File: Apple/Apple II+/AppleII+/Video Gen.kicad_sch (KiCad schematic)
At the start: 51 parts, among them J18 Aux Video, K14 VIDEO OUT, Q3 2N3904, Q6 2N3904

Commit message: less than 1000 errors to go
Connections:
- net GND: now also A9.8 (GND)
- net SOFT5: no longer A11.10 (~{S}), A11.13 (~{R}), A11.2 (D), A11.3 (C)
- net ~{RAS}: now also B5.1 (~{CLR}), B8.1 (~{CLR}), B8.1 (~{CLR})
- new net Soft5: A11.10 (~{S}), A11.13 (~{R}), A11.2 (D), A11.3 (C)
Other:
- note added: "James TODO: Verify these are wired correctly"
- note added: "James Todo: Is this 555 wired correclty"
- moved on the sheet: B3, B5A, B8A, B8F, C15, R13

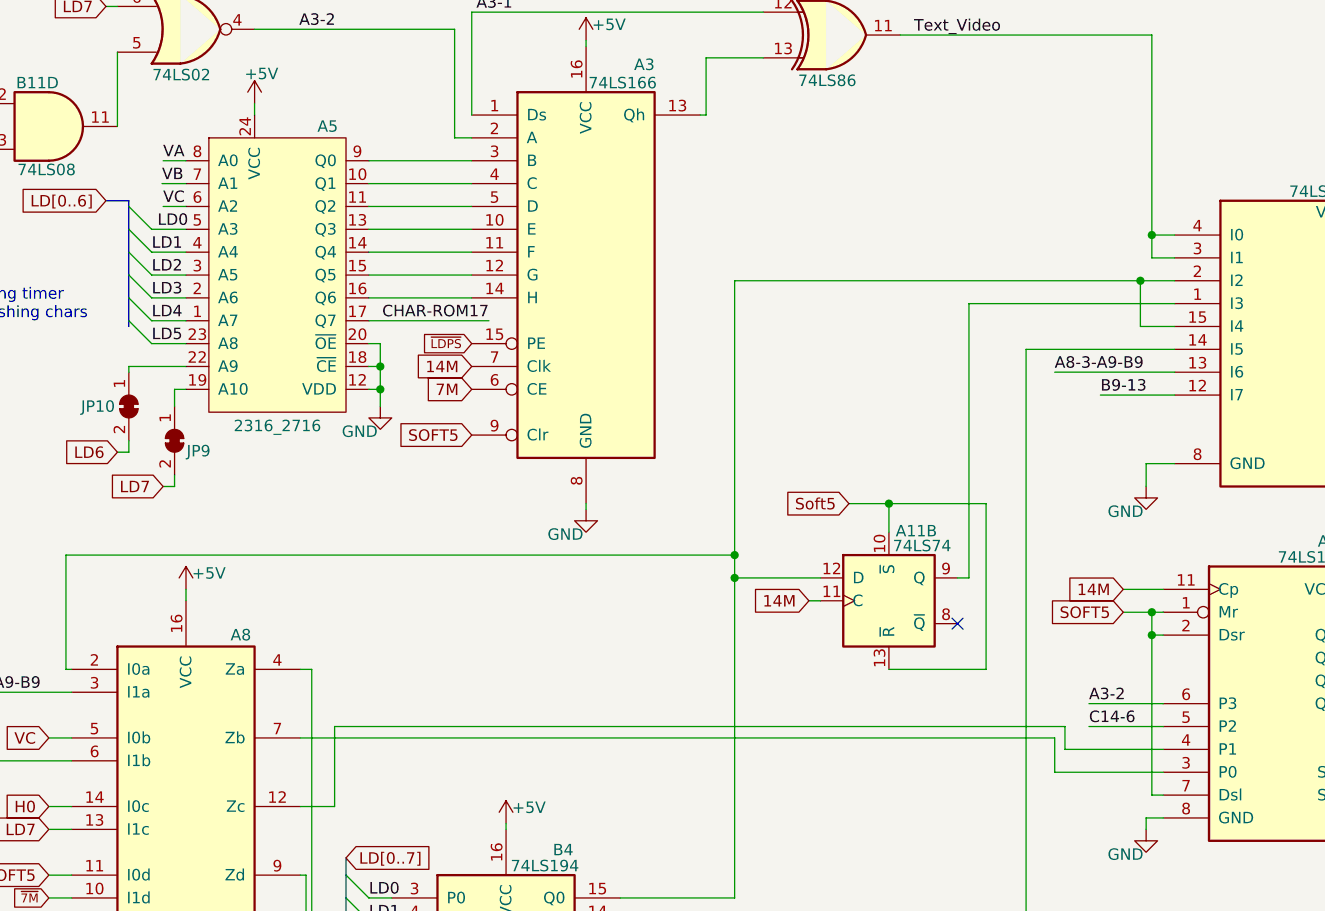
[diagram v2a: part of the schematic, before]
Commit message: cleaned most off-grid warnings
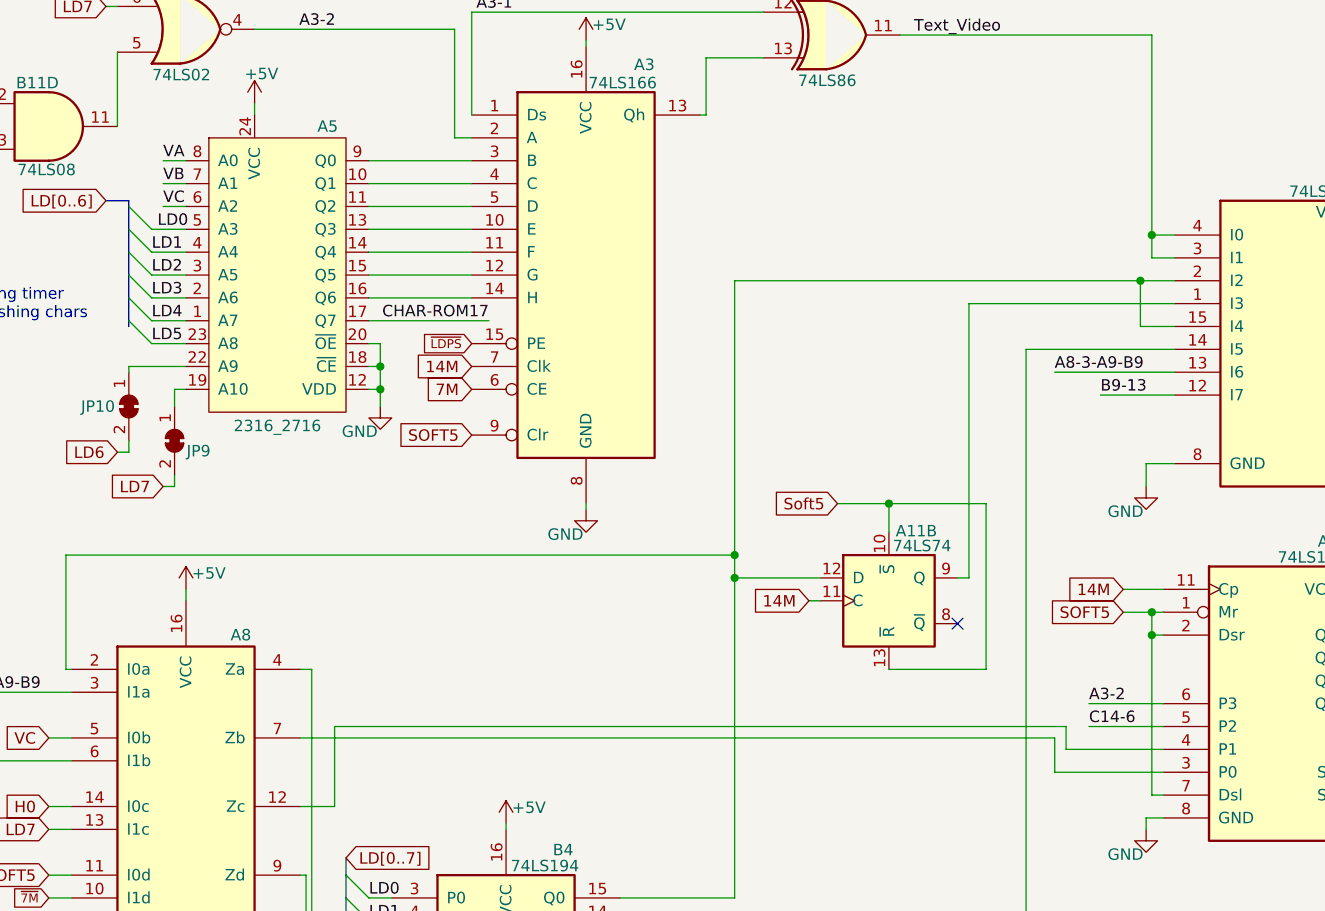
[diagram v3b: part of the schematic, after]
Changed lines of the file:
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@@
     (stroke (width 0) (type default))
   )
-  (wire (pts (xy 317.373 168.275) (xy 328.295 168.275))
+  (wire (pts (xy 317.5 168.275) (xy 328.295 168.275))
     (stroke (width 0) (type default))
   )
@@
     (stroke (width 0) (type default))
   )
-  (wire (pts (xy 217.043 105.41) (xy 219.71 105.41))
+  (wire (pts (xy 217.17 105.41) (xy 219.71 105.41))
     (stroke (width 0) (type default))
   )
@@
     (stroke (width 0) (type default))
   )
-  (wire (pts (xy 236.22 165.735) (xy 317.373 165.735))
+  (wire (pts (xy 236.22 165.735) (xy 317.5 165.735))
     (stroke (width 0) (type default))
   )
@@
     (stroke (width 0) (type default))
   )
-  (wire (pts (xy 293.37 140.97) (xy 297.815 140.97))
+  (wire (pts (xy 292.1 140.97) (xy 297.815 140.97))
     (stroke (width 0) (type default))
   )
@@
     (stroke (width 0) (type default))
   )
-  (wire (pts (xy 317.373 165.735) (xy 317.373 168.275))
+  (wire (pts (xy 317.5 165.735) (xy 317.5 168.275))
     (stroke (width 0) (type default))
   )
@@
     (effects (font (size 1.27 1.27)) (justify left bottom))
   )
-  (label "VB" (at 217.043 105.41 0) (fields_autoplaced)
+  (label "VB" (at 217.17 105.41 0) (fields_autoplaced)
     (effects (font (size 1.27 1.27)) (justify left bottom))
   )
@@
     )
   )
-  (global_label "Soft5" (shape input) (at 293.37 140.97 180)
-    (effects (font (size 1.27 1.27)) (justify right))
-    (property "Intersheetrefs" "${INTERSHEET_REFS}" (at 293.37 140.97 0)
-      (effects (font (size 1.27 1.27)) hide)
-    )
+  (global_label "Soft5" (shape input) (at 292.1 140.97 180)
+    (effects (font (size 1.27 1.27)) (justify right))
+    (property "Intersheetrefs" "${INTERSHEET_REFS}" (at 292.1 140.97 0)
+      (effects (font (size 1.27 1.27)) hide)
+    )

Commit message: Lots of ERC and minor fixes
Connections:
- net Soft5 is gone; now on net SOFT5: A11.10 (~{S}), A11.13 (~{R}), A11.2 (D), A11.3 (C)
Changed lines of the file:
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@@
+    (stroke (width 0) (type default))
+  )
+  (wire (pts (xy 214.63 102.235) (xy 214.63 102.87))
     (stroke (width 0) (type default))
   )
@@
     (stroke (width 0) (type default))
   )
-  (wire (pts (xy 66.675 78.105) (xy 67.945 78.105))
+  (wire (pts (xy 66.04 78.105) (xy 67.945 78.105))
     (stroke (width 0) (type default))
   )
@@
     (stroke (width 0) (type default))
   )
+  (wire (pts (xy 213.995 102.235) (xy 214.63 102.235))
+    (stroke (width 0) (type default))
+  )
   (wire (pts (xy 63.5 107.95) (xy 63.5 95.885))
     (stroke (width 0) (type default))
@@
     (stroke (width 0) (type default))
   )
-  (wire (pts (xy 217.17 105.41) (xy 219.71 105.41))
+  (wire (pts (xy 214.63 105.41) (xy 219.71 105.41))
     (stroke (width 0) (type default))
   )
@@
     (stroke (width 0) (type default))
   )
+  (wire (pts (xy 213.995 104.775) (xy 214.63 104.775))
+    (stroke (width 0) (type default))
+  )
   (wire (pts (xy 292.1 140.97) (xy 297.815 140.97))
     (stroke (width 0) (type default))
@@
     (stroke (width 0) (type default))
   )
-  (wire (pts (xy 217.17 102.87) (xy 219.71 102.87))
+  (wire (pts (xy 214.63 102.87) (xy 219.71 102.87))
     (stroke (width 0) (type default))
   )
@@
     (stroke (width 0) (type default))
   )
-  (wire (pts (xy 66.675 73.025) (xy 67.945 73.025))
+  (wire (pts (xy 66.04 73.025) (xy 67.945 73.025))
     (stroke (width 0) (type default))
   )
@@
   )
   (wire (pts (xy 240.03 187.325) (xy 242.57 187.325))
+    (stroke (width 0) (type default))
+  )
+  (wire (pts (xy 214.63 104.775) (xy 214.63 105.41))
     (stroke (width 0) (type default))
   )
@@
     )
   )
-  (global_label "V4" (shape input) (at 66.675 78.105 180)
-    (effects (font (size 1.27 1.27)) (justify right))
-    (property "Intersheetrefs" "${INTERSHEET_REFS}" (at 66.675 78.105 0)
+  (global_label "V4" (shape input) (at 66.04 78.105 180)
+    (effects (font (size 1.27 1.27)) (justify right))
+    (property "Intersheetrefs" "${INTERSHEET_REFS}" (at 66.04 78.105 0)
       (effects (font (size 1.27 1.27)) hide)
     )
@@
     )
   )
-  (global_label "V3" (shape input) (at 66.675 73.025 180)
-    (effects (font (size 1.27 1.27)) (justify right))
-    (property "Intersheetrefs" "${INTERSHEET_REFS}" (at 66.675 73.025 0)
+  (global_label "V3" (shape input) (at 66.04 73.025 180)
+    (effects (font (size 1.27 1.27)) (justify right))
+    (property "Intersheetrefs" "${INTERSHEET_REFS}" (at 66.04 73.025 0)
       (effects (font (size 1.27 1.27)) hide)
     )
@@
     )
   )
+  (global_label "VA" (shape input) (at 213.995 102.235 180)
+    (effects (font (size 1.27 1.27)) (justify right))
+    (property "Intersheetrefs" "${INTERSHEET_REFS}" (at 213.995 102.235 0)
+      (effects (font (size 1.27 1.27)) hide)
+    )
+  )
   (global_label "SOFT5-A2-8" (shape output) (at 50.165 248.285 0)
     (effects (font (size 1.27 1.27)) (justify left))
@@
     )
   )
-  (global_label "Soft5" (shape input) (at 180.34 184.785 180)
+  (global_label "SOFT5" (shape input) (at 180.34 184.785 180)
     (effects (font (size 1.27 1.27)) (justify right))
     (property "Intersheetrefs" "${INTERSHEET_REFS}" (at 180.34 184.785 0)
@@
     )
   )
-  (global_label "Soft5" (shape input) (at 292.1 140.97 180)
+  (global_label "SOFT5" (shape input) (at 292.1 140.97 180)
     (effects (font (size 1.27 1.27)) (justify right))
     (property "Intersheetrefs" "${INTERSHEET_REFS}" (at 292.1 140.97 0)
@@
     (effects (font (size 1.27 1.27)) (justify left))
     (property "Intersheetrefs" "${INTERSHEET_REFS}" (at 129.54 115.57 0)
+      (effects (font (size 1.27 1.27)) hide)
+    )
+  )
+  (global_label "VB" (shape input) (at 213.995 104.775 180)
+    (effects (font (size 1.27 1.27)) (justify right))
+    (property "Intersheetrefs" "${INTERSHEET_REFS}" (at 213.995 104.775 0)
       (effects (font (size 1.27 1.27)) hide)
     )
@@
     )
   )
-  (symbol (lib_name "74LS174_1") (lib_id "AppleII+:74LS174") (at 117.475 190.5 0) (unit 6)
+  (symbol (lib_id "AppleII+:74LS174") (at 117.475 190.5 0) (unit 6)
     (in_bom yes) (on_board yes) (dnp no)
     (property "Reference" "B8" (at 119.253 185.928 0)

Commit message: Started moving Global labels to Hierarchical and Local labels
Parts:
- C15, Cap13, Cap14: value 0.1uf -> 100n
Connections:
- net LD6: now also JP10.1 (A); no longer JP10.2 (B)
- net LD7: now also JP9.1 (A); no longer JP9.2 (B)
- net at A5.19 (A10): now also JP9.2 (B); no longer JP9.1 (A)
- net at A5.22 (A9): now also JP10.2 (B); no longer JP10.1 (A)
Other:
- moved on the sheet: A10, A11A, A11B, A12B, A12C, A12D, A2C, A2D, A3, A5, A8, A9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

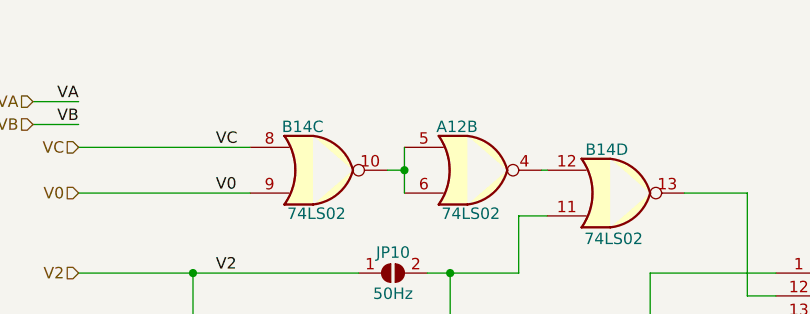
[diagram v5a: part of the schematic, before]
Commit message: Changed global labels to hierachry and started front page changes
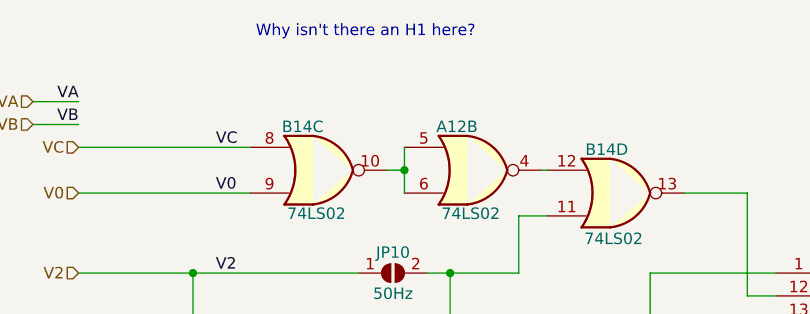
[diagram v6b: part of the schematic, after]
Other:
- note added: "Why isn't there an H1 here?"
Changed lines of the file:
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@@
     (effects (font (size 1.27 1.27) (color 255 153 0 1)) (justify left bottom))
+  )
+  (text "Why isn't there an H1 here?" (at 46.99 16.51 0)
+    (effects (font (size 1.27 1.27)) (justify left bottom))
   )
   (text "James Todo: Is this 555 wired correclty" (at 179.705 149.225 0)

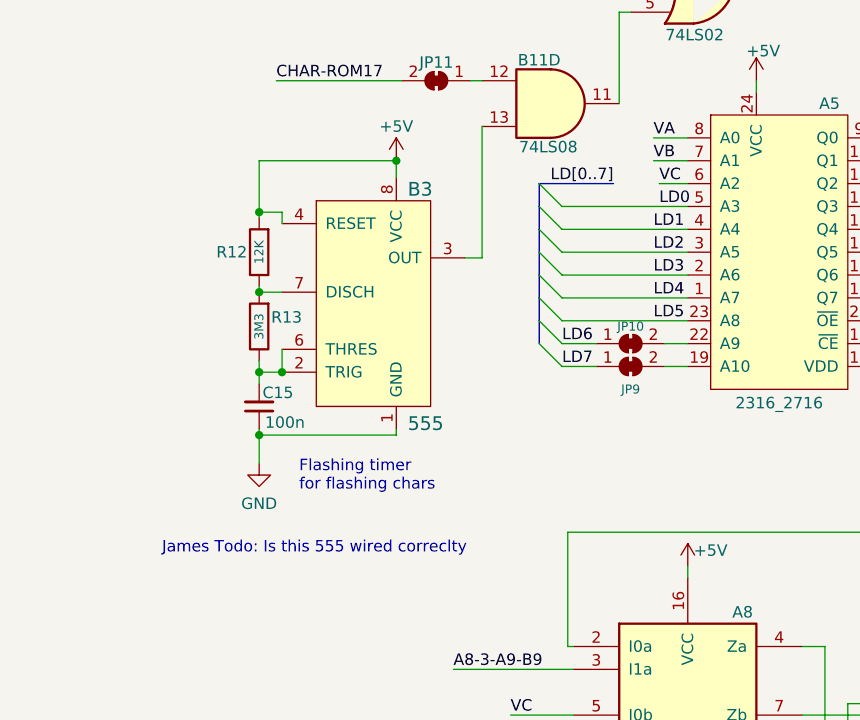
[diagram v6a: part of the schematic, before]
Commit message: Fixed CAS and A6 on RAM page (plus lots of other clean ups)
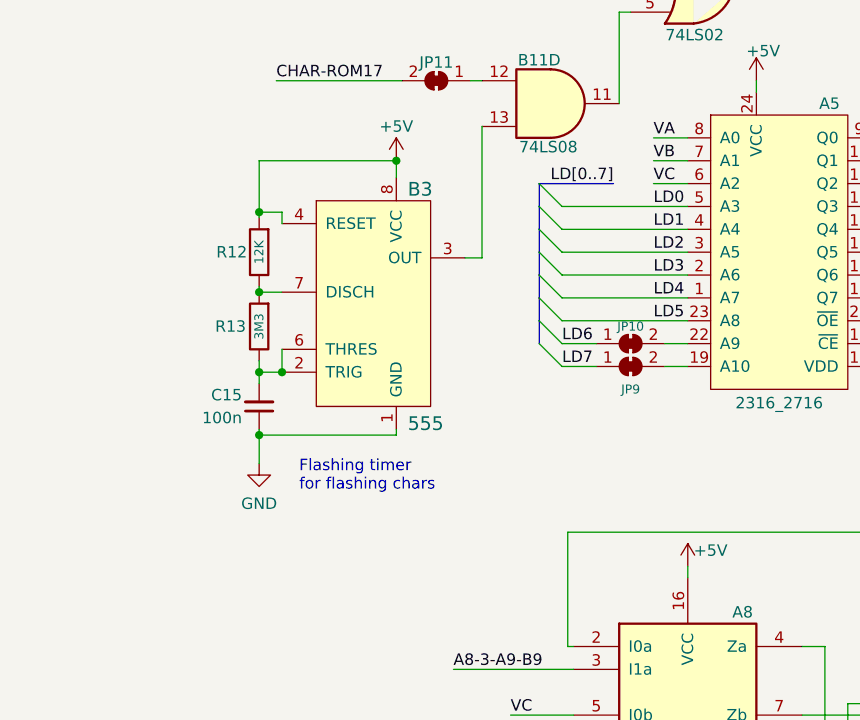
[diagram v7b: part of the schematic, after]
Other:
- note removed: "James Todo: Is this 555 wired correclty"
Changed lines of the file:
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@@
     (stroke (width 0) (type default))
   )
-  (wire (pts (xy 234.95 107.95) (xy 238.125 107.95))
+  (wire (pts (xy 234.315 107.95) (xy 238.125 107.95))
     (stroke (width 0) (type default))
   )
@@
     (stroke (width 0) (type default))
   )
-  (wire (pts (xy 224.155 110.49) (xy 238.125 110.49))
-    (stroke (width 0) (type default))
-  )
   (bus (pts (xy 255.905 180.34) (xy 255.905 182.245))
     (stroke (width 0) (type default))
@@
     (stroke (width 0) (type default))
   )
+  (wire (pts (xy 224.155 110.49) (xy 238.125 110.49))
+    (stroke (width 0) (type default))
+  )
   (wire (pts (xy 190.5 127.635) (xy 190.5 128.905))
     (stroke (width 0) (type default))
@@
     (effects (font (size 1.27 1.27)) (justify left bottom))
   )
-  (text "James Todo: Is this 555 wired correclty" (at 179.705 149.225 0)
-    (effects (font (size 1.27 1.27) (color 255 153 0 1)) (justify left bottom))
-  )
   (text "Flashing timer\nfor flashing chars" (at 194.945 142.24 0)
     (effects (font (size 1.27 1.27)) (justify left bottom))
@@
     (effects (font (size 1.27 1.27)) (justify left bottom))
   )
-  (label "LD0" (at 234.95 110.49 0) (fields_autoplaced)
+  (label "LD0" (at 234.315 110.49 0) (fields_autoplaced)
     (effects (font (size 1.27 1.27)) (justify left bottom))
   )
@@
     (effects (font (size 1.27 1.27)) (justify left bottom))
   )
-  (label "VC" (at 234.95 107.95 0) (fields_autoplaced)
+  (label "VC" (at 234.315 107.95 0) (fields_autoplaced)
     (effects (font (size 1.27 1.27)) (justify left bottom))
   )
@@
   (symbol (lib_id "Device:R") (at 190.5 123.825 180) (unit 1)
     (in_bom yes) (on_board yes) (dnp no)
-    (property "Reference" "R13" (at 193.548 122.809 0)
+    (property "Reference" "R13" (at 187.325 123.825 0)
       (effects (font (size 1.27 1.27)))
     )
@@
   (symbol (lib_id "Device:C_Small") (at 190.5 132.715 180) (unit 1)
     (in_bom yes) (on_board yes) (dnp no)
-    (property "Reference" "C15" (at 194.31 131.191 0)
+    (property "Reference" "C15" (at 188.595 131.445 0)
       (effects (font (size 1.27 1.27)) (justify left))
     )
-    (property "Value" "100n" (at 195.58 134.493 0)
+    (property "Value" "100n" (at 188.595 133.985 0)
       (effects (font (size 1.27 1.27)) (justify left))
     )
